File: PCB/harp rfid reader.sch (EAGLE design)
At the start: 41 parts, among them IC1 FT232RL, IC2 LP5907MFX-3.3, IC3 ATXMEGA32A4U-AU, Q1 BC817-40W, U1 ID-12/20SMD

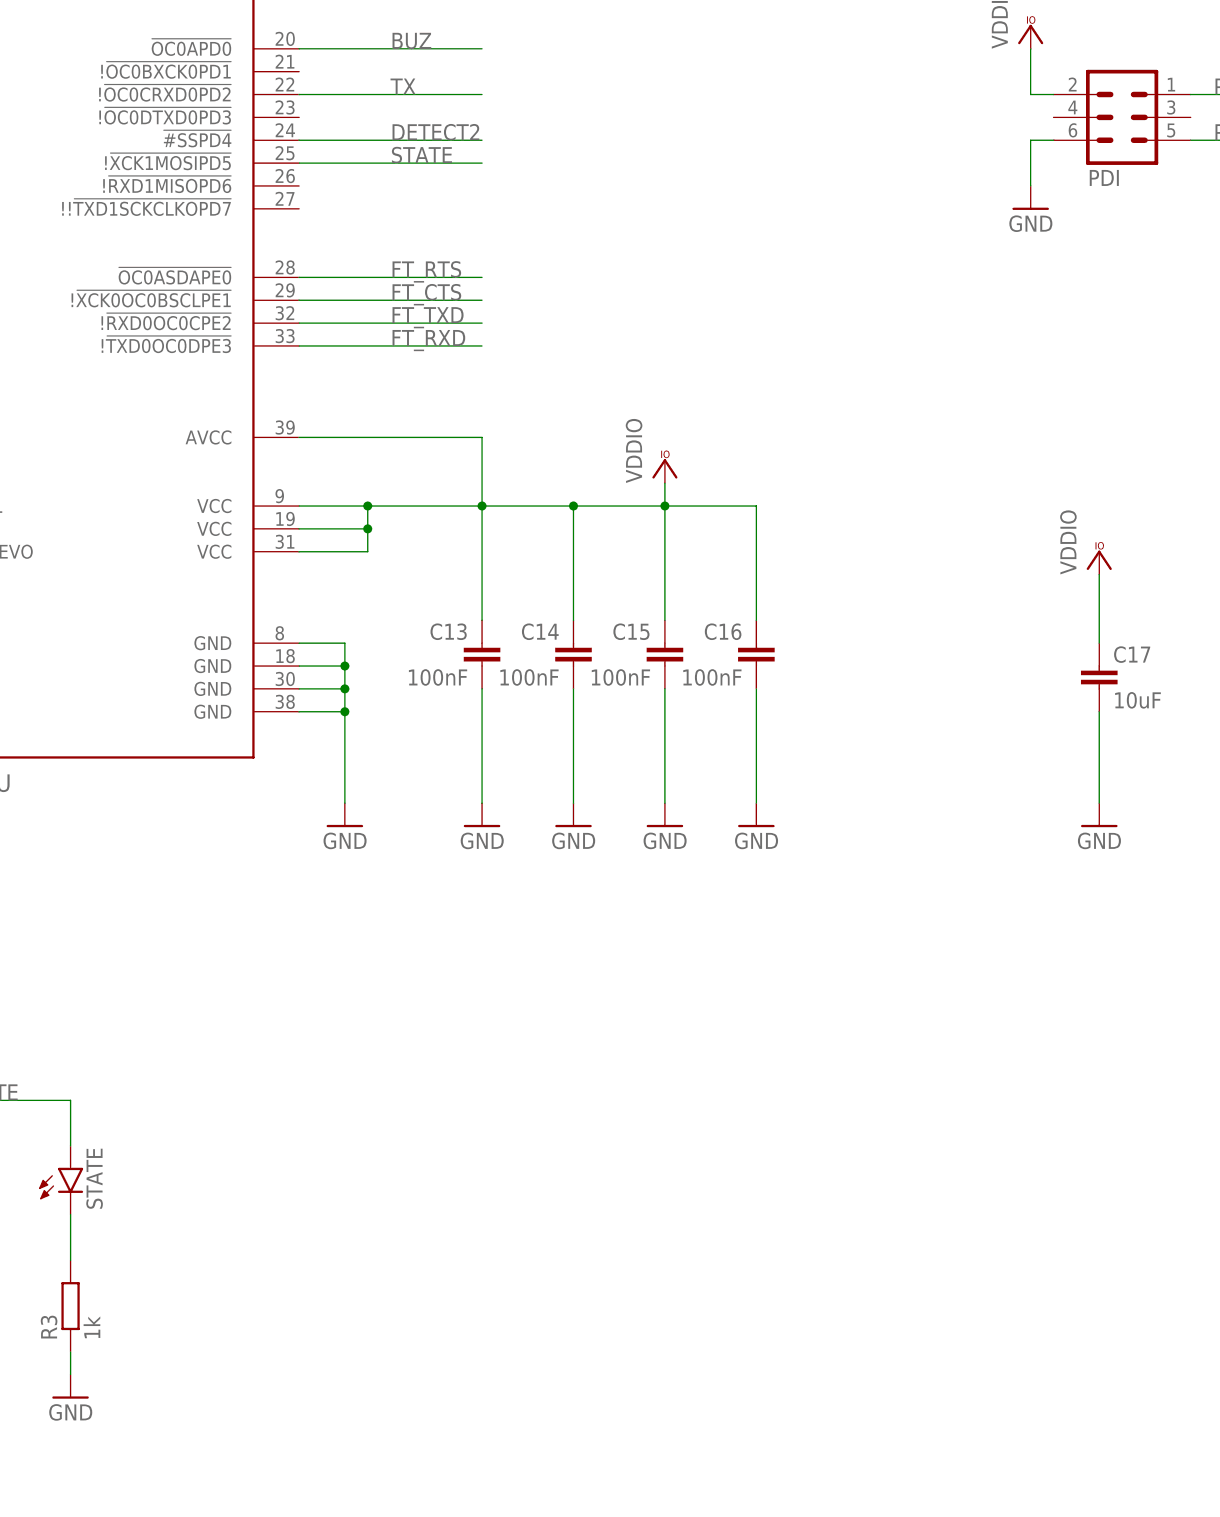
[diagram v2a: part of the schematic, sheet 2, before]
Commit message: Added a digital output.
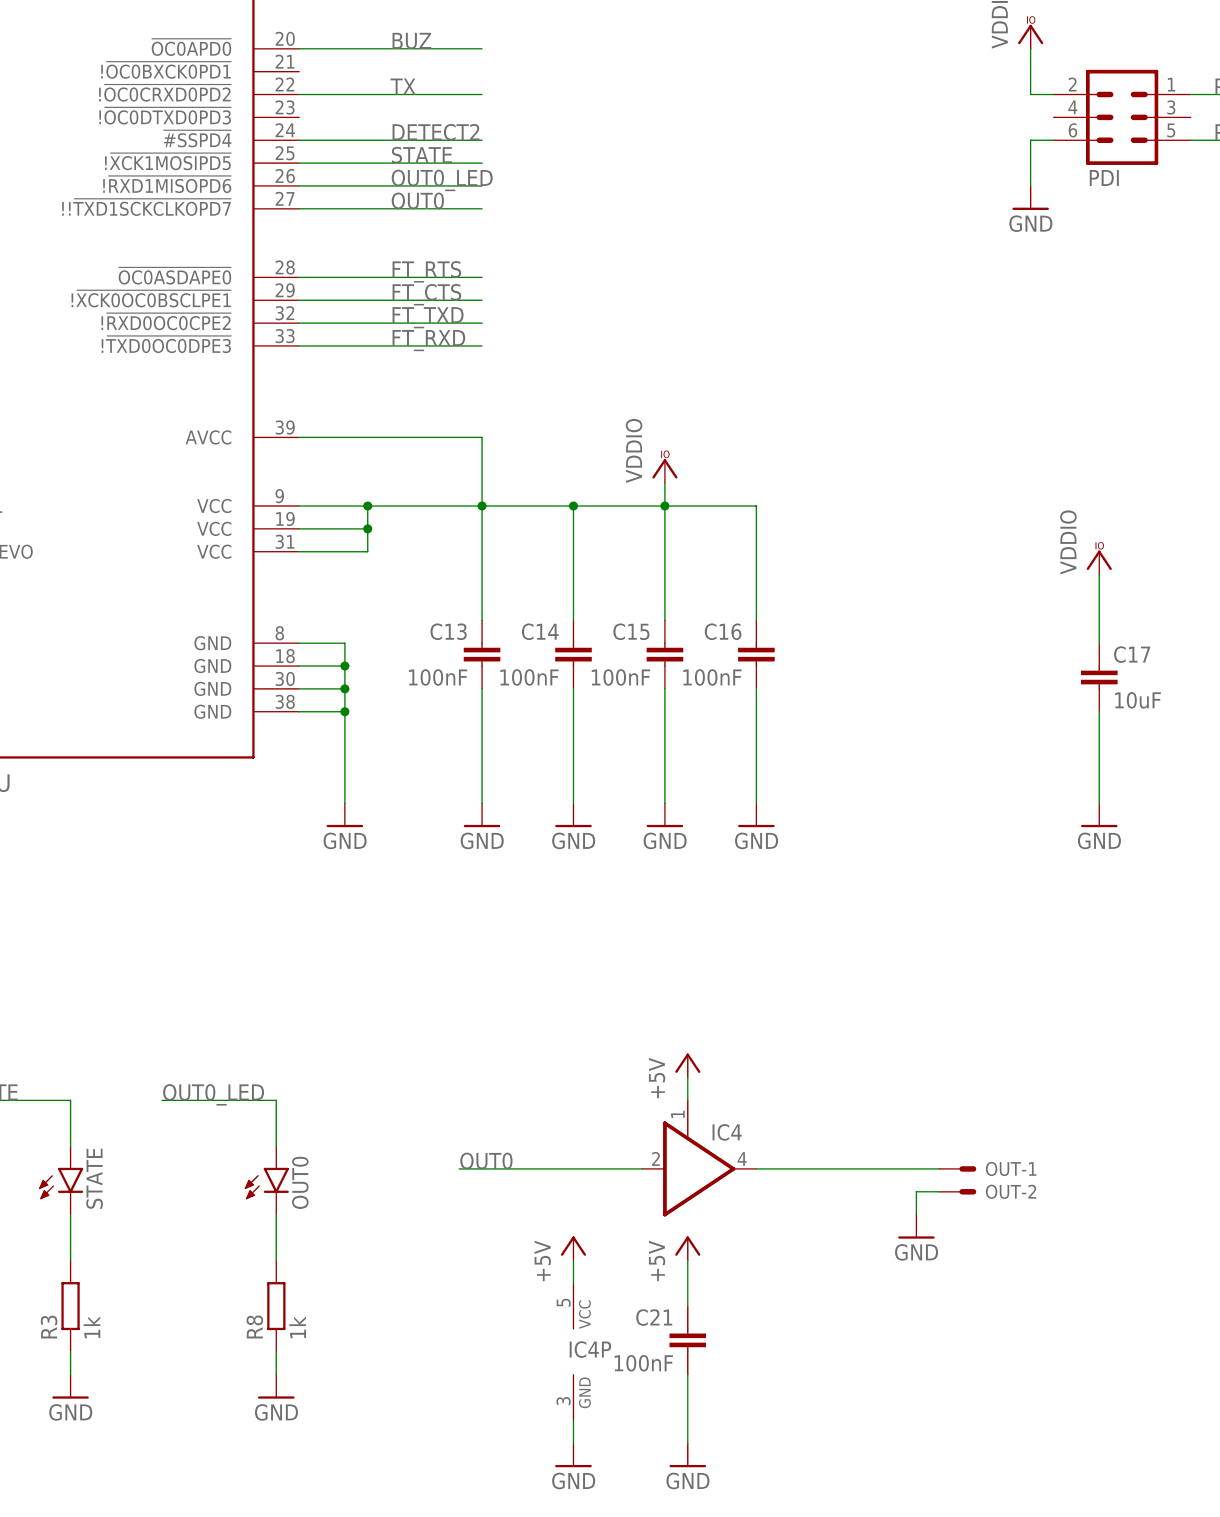
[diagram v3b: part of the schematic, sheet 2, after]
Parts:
- added C21: 100nF, rcl:C-EUC0402
- added IC4: 74AHC1G126DBV, 74xx-little-de:74AHC1G126DBV
- added OUT: 22-23-2021, con-molex:22-23-2021
- added OUT0: (no value), led:LEDCHIP-LED0603
- added R8: 1k, rcl:R-EU_R0402
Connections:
- new net N$6: OUT0.C, R8.2
- new net N$7: IC4A.O, OUT-1.S
- new net OUT0: IC3.!!!TXD1SCKCLKOPD7, IC4A.I
- new net OUT0_LED: IC3.!!RXD1MISOPD6, OUT0.A
- net +5V: now also C21.1, IC4A.OE, IC4P.VCC
- net GND: now also C21.2, IC4P.GND, OUT-2.S, R8.1
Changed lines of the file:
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@@
 <layer number="112" name="tSilk" color="7" fill="1" visible="yes" active="yes"/>
 <layer number="113" name="IDFDebug" color="4" fill="1" visible="yes" active="yes"/>
+<layer number="114" name="Badge_Outline" color="7" fill="1" visible="yes" active="yes"/>
+<layer number="115" name="ReferenceISLANDS" color="7" fill="1" visible="yes" active="yes"/>
 <layer number="116" name="Patch_BOT" color="9" fill="4" visible="yes" active="yes"/>
 <layer number="118" name="RECTANGLE_PADS" color="4" fill="1" visible="yes" active="yes"/>
@@
 <part name="P+4" library="supply1" deviceset="+5V" device=""/>
 <part name="GND13" library="supply1" deviceset="GND" device=""/>
+<part name="IC4" library="74xx-little-de" deviceset="74*1G126" device="DBV" technology="AHC" value=""/>
+<part name="P+5" library="supply1" deviceset="+5V" device=""/>
+<part name="GND14" library="supply1" deviceset="GND" device=""/>
+<part name="C21" library="rcl" deviceset="C-EU" device="C0402" value="100nF"/>
+<part name="P+6" library="supply1" deviceset="+5V" device=""/>
+<part name="GND15" library="supply1" deviceset="GND" device=""/>
+<part name="OUT" library="con-molex" deviceset="22-23-2021" device=""/>
+<part name="GND16" library="supply1" deviceset="GND" device=""/>
+<part name="OUT0" library="led" library_urn="urn:adsk.eagle:library:259" deviceset="LED" device="CHIP-LED0603" package3d_urn="urn:adsk.eagle:package:15819/3"/>
+<part name="R8" library="rcl" library_urn="urn:adsk.eagle:library:334" deviceset="R-EU_" device="R0402" package3d_urn="urn:adsk.eagle:package:23547/3" value="1k"/>
+<part name="GND17" library="supply1" deviceset="GND" device=""/>
+<part name="P+7" library="supply1" deviceset="+5V" device=""/>
 </parts>
 <sheets>
@@
 <instance part="GND13" gate="1" x="25.4" y="132.08" smashed="yes" rot="MR0">
 <attribute name="VALUE" x="27.94" y="129.54" size="1.778" layer="96" rot="MR0"/>
+</instance>
+<instance part="IC4" gate="A" x="302.26" y="78.74" smashed="yes">
+<attribute name="NAME" x="304.8" y="81.915" size="1.778" layer="95"/>
+<attribute name="VALUE" x="304.8" y="73.66" size="1.778" layer="96"/>
+</instance>
+<instance part="IC4" gate="P" x="289.56" y="58.42" smashed="yes">
+<attribute name="NAME" x="288.925" y="57.785" size="1.778" layer="95"/>
+</instance>
+<instance part="P+5" gate="1" x="289.56" y="71.12" smashed="yes">
+<attribute name="VALUE" x="287.02" y="66.04" size="1.778" layer="96" rot="R90"/>
+</instance>
+<instance part="GND14" gate="1" x="289.56" y="45.72" smashed="yes" rot="MR0">
+<attribute name="VALUE" x="292.1" y="43.18" size="1.778" layer="96" rot="MR0"/>
+</instance>
+<instance part="C21" gate="G$1" x="302.26" y="60.96" smashed="yes" rot="MR0">
+<attribute name="NAME" x="300.736" y="61.341" size="1.778" layer="95" rot="MR0"/>
+<attribute name="VALUE" x="300.736" y="56.261" size="1.778" layer="96" rot="MR0"/>
+</instance>
+<instance part="P+6" gate="1" x="302.26" y="71.12" smashed="yes">
+<attribute name="VALUE" x="299.72" y="66.04" size="1.778" layer="96" rot="R90"/>
+</instance>
+<instance part="GND15" gate="1" x="302.26" y="45.72" smashed="yes" rot="MR0">
+<attribute name="VALUE" x="304.8" y="43.18" size="1.778" layer="96" rot="MR0"/>
+</instance>
+<instance part="OUT" gate="-1" x="332.74" y="78.74" smashed="yes">
+<attribute name="NAME" x="335.28" y="77.978" size="1.524" layer="95"/>
+</instance>
+<instance part="OUT" gate="-2" x="332.74" y="76.2" smashed="yes">
+<attribute name="NAME" x="335.28" y="75.438" size="1.524" layer="95"/>
+</instance>
+<instance part="GND16" gate="1" x="327.66" y="71.12" smashed="yes" rot="MR0">
+<attribute name="VALUE" x="330.2" y="68.58" size="1.778" layer="96" rot="MR0"/>
+</instance>
+<instance part="OUT0" gate="G$1" x="256.54" y="78.74" smashed="yes">
+<attribute name="NAME" x="260.096" y="74.168" size="1.778" layer="95" rot="R90"/>
+<attribute name="VALUE" x="262.255" y="74.168" size="1.778" layer="96" rot="R90"/>
+</instance>
+<instance part="R8" gate="G$1" x="256.54" y="63.5" smashed="yes" rot="R90">
+<attribute name="NAME" x="255.0414" y="59.69" size="1.778" layer="95" rot="R90"/>
+<attribute name="VALUE" x="259.842" y="59.69" size="1.778" layer="96" rot="R90"/>
+</instance>
+<instance part="GND17" gate="1" x="256.54" y="53.34" smashed="yes" rot="MR0">
+<attribute name="VALUE" x="259.08" y="50.8" size="1.778" layer="96" rot="MR0"/>
+</instance>
+<instance part="P+7" gate="1" x="302.26" y="91.44" smashed="yes">
+<attribute name="VALUE" x="299.72" y="86.36" size="1.778" layer="96" rot="R90"/>
 </instance>
 </instances>
@@
 <wire x1="25.4" y1="134.62" x2="25.4" y2="137.16" width="0.1524" layer="91"/>
 </segment>
+<segment>
+<pinref part="IC4" gate="P" pin="GND"/>
+<pinref part="GND14" gate="1" pin="GND"/>
+<wire x1="289.56" y1="50.8" x2="289.56" y2="48.26" width="0.1524" layer="91"/>
+</segment>
+<segment>
+<pinref part="C21" gate="G$1" pin="2"/>
+<pinref part="GND15" gate="1" pin="GND"/>
+<wire x1="302.26" y1="55.88" x2="302.26" y2="48.26" width="0.1524" layer="91"/>
+</segment>
+<segment>
+<pinref part="OUT" gate="-2" pin="S"/>
+<wire x1="330.2" y1="76.2" x2="327.66" y2="76.2" width="0.1524" layer="91"/>
+<pinref part="GND16" gate="1" pin="GND"/>
+<wire x1="327.66" y1="76.2" x2="327.66" y2="73.66" width="0.1524" layer="91"/>
+</segment>
+<segment>
+<pinref part="R8" gate="G$1" pin="1"/>
+<pinref part="GND17" gate="1" pin="GND"/>
+<wire x1="256.54" y1="58.42" x2="256.54" y2="55.88" width="0.1524" layer="91"/>
+</segment>
 </net>
 <net name="OSC1" class="0">
@@
 <pinref part="C20" gate="G$1" pin="+"/>
 <wire x1="25.4" y1="147.32" x2="25.4" y2="144.78" width="0.1524" layer="91"/>
+</segment>
+<segment>
+<pinref part="P+5" gate="1" pin="+5V"/>
+<pinref part="IC4" gate="P" pin="VCC"/>
+<wire x1="289.56" y1="68.58" x2="289.56" y2="66.04" width="0.1524" layer="91"/>
+</segment>
+<segment>
+<pinref part="C21" gate="G$1" pin="1"/>
+<pinref part="P+6" gate="1" pin="+5V"/>
+<wire x1="302.26" y1="63.5" x2="302.26" y2="68.58" width="0.1524" layer="91"/>
+</segment>
+<segment>
+<pinref part="IC4" gate="A" pin="OE"/>
+<wire x1="302.26" y1="86.36" x2="302.26" y2="88.9" width="0.1524" layer="91"/>
+<pinref part="P+7" gate="1" pin="+5V"/>
 </segment>
 </net>
@@
 </segment>
 </net>
+<net name="OUT0" class="0">
+<segment>
+<pinref part="IC3" gate="G$1" pin="!!!TXD1SCKCLKOPD7"/>
+<wire x1="259.08" y1="185.42" x2="279.4" y2="185.42" width="0.1524" layer="91"/>
+<label x="269.24" y="185.42" size="1.778" layer="95"/>
+</segment>
+<segment>
+<pinref part="IC4" gate="A" pin="I"/>
+<wire x1="297.18" y1="78.74" x2="276.86" y2="78.74" width="0.1524" layer="91"/>
+<label x="276.86" y="78.74" size="1.778" layer="95"/>
+</segment>
+</net>
+<net name="N$7" class="0">
+<segment>
+<pinref part="IC4" gate="A" pin="O"/>
+<pinref part="OUT" gate="-1" pin="S"/>
+<wire x1="330.2" y1="78.74" x2="309.88" y2="78.74" width="0.1524" layer="91"/>
+</segment>
+</net>
+<net name="N$6" class="0">
+<segment>
+<pinref part="OUT0" gate="G$1" pin="C"/>
+<pinref part="R8" gate="G$1" pin="2"/>
+<wire x1="256.54" y1="73.66" x2="256.54" y2="68.58" width="0.1524" layer="91"/>
+</segment>
+</net>
+<net name="OUT0_LED" class="0">
+<segment>
+<pinref part="OUT0" gate="G$1" pin="A"/>
+<wire x1="256.54" y1="81.28" x2="256.54" y2="86.36" width="0.1524" layer="91"/>
+<wire x1="256.54" y1="86.36" x2="243.84" y2="86.36" width="0.1524" layer="91"/>
+<label x="243.84" y="86.36" size="1.778" layer="95"/>
+</segment>
+<segment>
+<pinref part="IC3" gate="G$1" pin="!!RXD1MISOPD6"/>
+<wire x1="259.08" y1="187.96" x2="279.4" y2="187.96" width="0.1524" layer="91"/>
+<label x="269.24" y="187.96" size="1.778" layer="95"/>
+</segment>
+</net>
